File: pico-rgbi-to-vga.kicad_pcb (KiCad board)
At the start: 2 copper layers, 69 x 52 mm, 3 parts, among them J1 SDS-80J, J2 DB15_Female_HighDensity, U1 Pico

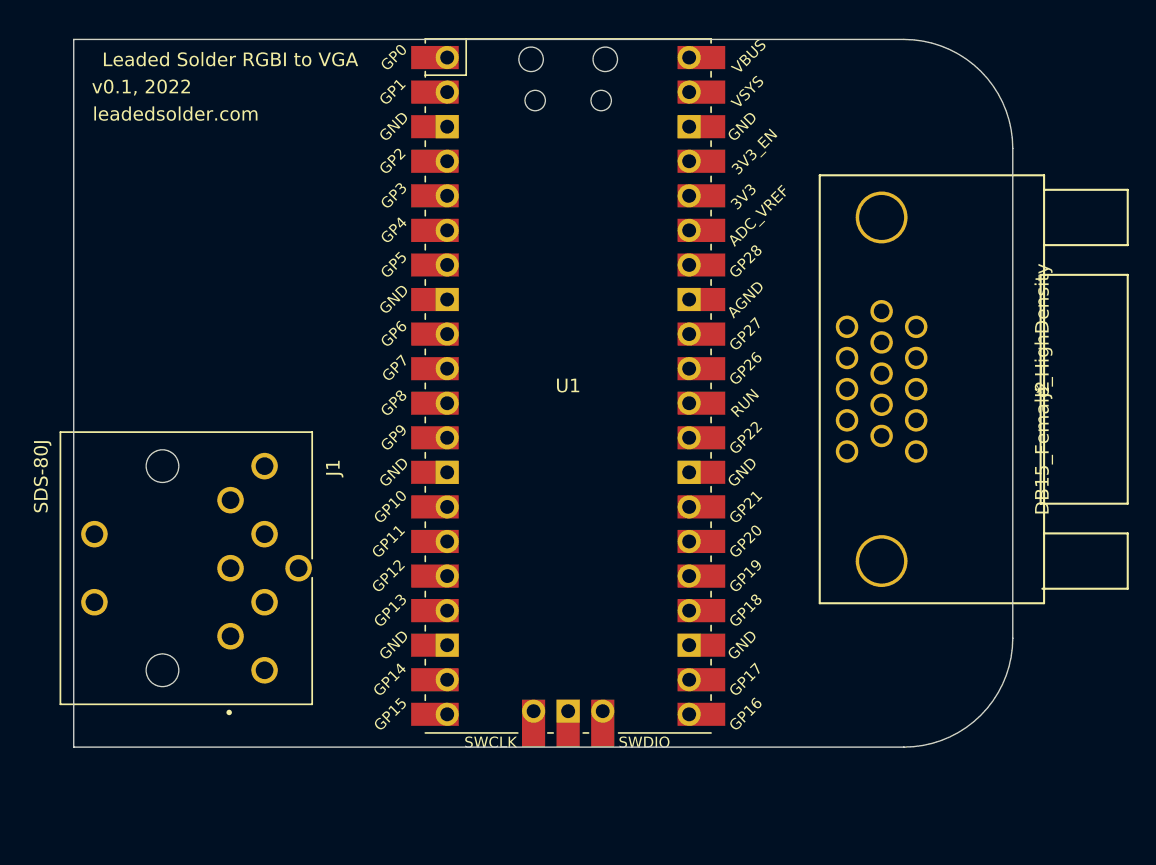
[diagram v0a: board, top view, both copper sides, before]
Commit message: Ground plane, bigger board
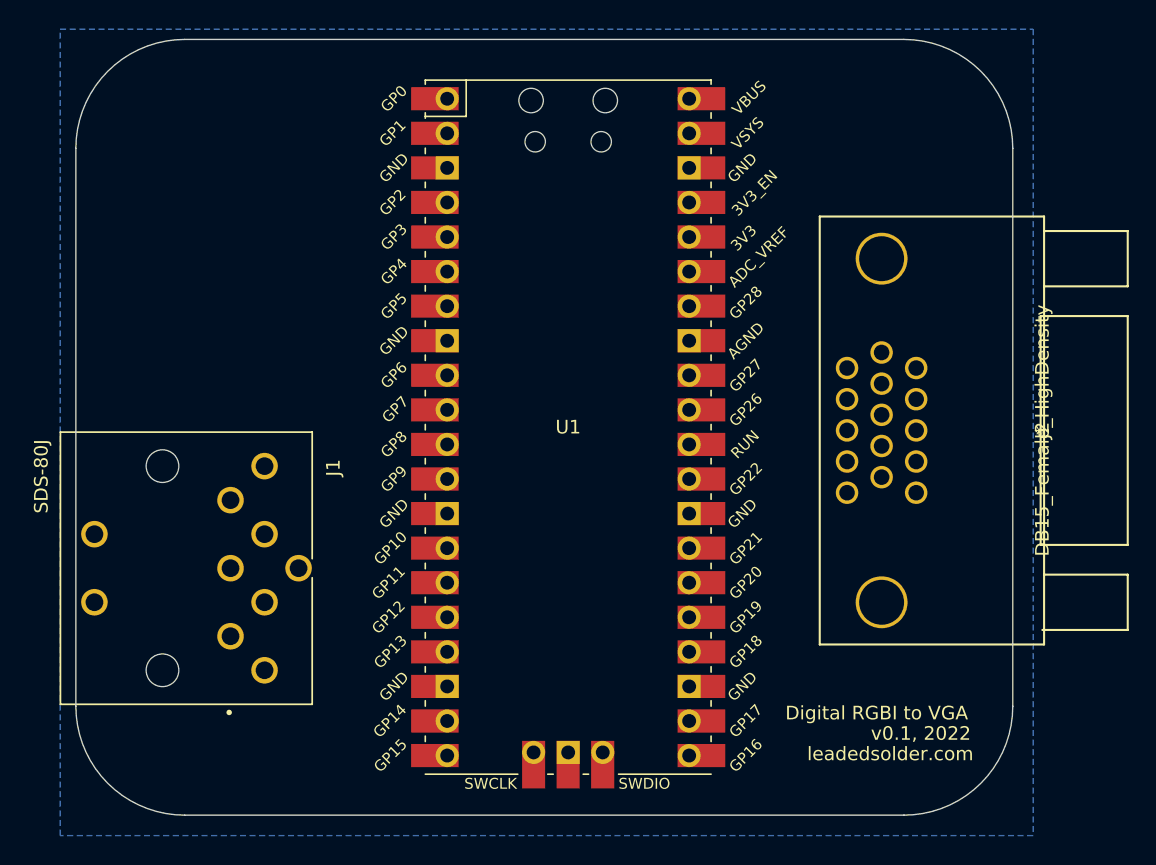
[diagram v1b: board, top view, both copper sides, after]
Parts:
- moved J2 3.03 mm to (172.2, 91.7)
- moved U1 3.03 mm to (137.3, 91.5)
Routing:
- added copper zone on B.Cu, net GND
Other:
- board size 69 x 52 mm -> 68.8 x 57 mm
- board text added: "Digital RGBI to VGA"
- board text removed: "Leaded Solder RGBI to VGA"
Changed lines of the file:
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@@
   (net 51 "unconnected-(U1-Pad43)")
   (footprint "MCU_RaspberryPi_and_Boards:RPi_Pico_SMD_TH" (layer "F.Cu")
-    (at 137.332 88.461)
+    (at 137.332 91.49)
     (descr "Through hole straight pin header, 2x20, 2.54mm pitch, double rows")
     (tags "Through hole pin header THT 2x20 2.54mm double row")
@@
   )
   (footprint "Connector_TE_AMP_HD15:FIXED-1-1734530-1" (layer "F.Cu")
-    (at 172.1739 88.706 -90)
+    (at 172.1739 91.735 -90)
     (property "Sheetfile" "pico-rgbi-to-vga.kicad_sch")
     (property "Sheetname" "")
@@
       (net 2 "GND") (pinfunction "SHIELD") (pintype "passive"))
   )
-  (gr_line (start 170 71) (end 170 107) (layer "Edge.Cuts") (width 0.1))
-  (gr_line (start 101 115) (end 101 63) (layer "Edge.Cuts") (width 0.1))
-  (gr_arc (start 170 107) (mid 167.656854 112.656854) (end 162 115) (layer "Edge.Cuts") (width 0.1))
-  (gr_line (start 162 115) (end 101 115) (layer "Edge.Cuts") (width 0.1))
-  (gr_line (start 162 63) (end 101 63) (layer "Edge.Cuts") (width 0.1))
+  (gr_arc (start 109.156854 120) (mid 103.5 117.656854) (end 101.156854 112) (layer "Edge.Cuts") (width 0.1))
+  (gr_arc (start 101.156854 70.999999) (mid 103.5 65.343145) (end 109.156854 62.999999) (layer "Edge.Cuts") (width 0.1))
+  (gr_line (start 101.156854 70.999999) (end 101.156854 112) (layer "Edge.Cuts") (width 0.1))
+  (gr_line (start 109.156854 62.999999) (end 162 63) (layer "Edge.Cuts") (width 0.1))
+  (gr_arc (start 170 112) (mid 167.656854 117.656854) (end 162 120) (layer "Edge.Cuts") (width 0.1))
+  (gr_line (start 162 120) (end 109.156854 120) (layer "Edge.Cuts") (width 0.1))
   (gr_arc (start 162 63) (mid 167.656854 65.343146) (end 170 71) (layer "Edge.Cuts") (width 0.1))
-  (gr_text "v0.1, 2022" (at 106 66.5) (layer "F.SilkS")
+  (gr_line (start 170 71) (end 170 112) (layer "Edge.Cuts") (width 0.1))
+  (gr_text "v0.1, 2022" (at 163.25 114) (layer "F.SilkS")
     (effects (font (size 1 1) (thickness 0.15)))
   )
-  (gr_text "Leaded Solder RGBI to VGA" (at 112.5 64.5) (layer "F.SilkS")
+  (gr_text "Digital RGBI to VGA" (at 160 112.5) (layer "F.SilkS")
     (effects (font (size 1 1) (thickness 0.15)))
   )
-  (gr_text "leadedsolder.com" (at 108.5 68.5) (layer "F.SilkS")
+  (gr_text "leadedsolder.com" (at 161 115.5) (layer "F.SilkS")
     (effects (font (size 1 1) (thickness 0.15)))
   )
+  (zone (net 2) (net_name "GND") (layer "B.Cu") (hatch edge 0.508)
+    (connect_pads yes (clearance 0.508))
+    (min_thickness 0.254) (filled_areas_thickness no)
+    (fill yes (thermal_gap 0.508) (thermal_bridge_width 0.508))
+    (polygon
+      (pts
+        (xy 171.5 121.5)
+        (xy 100 121.5)
+        (xy 100 62.25)
+        (xy 171.5 62.25)
+      )
+    )
+  )
 )

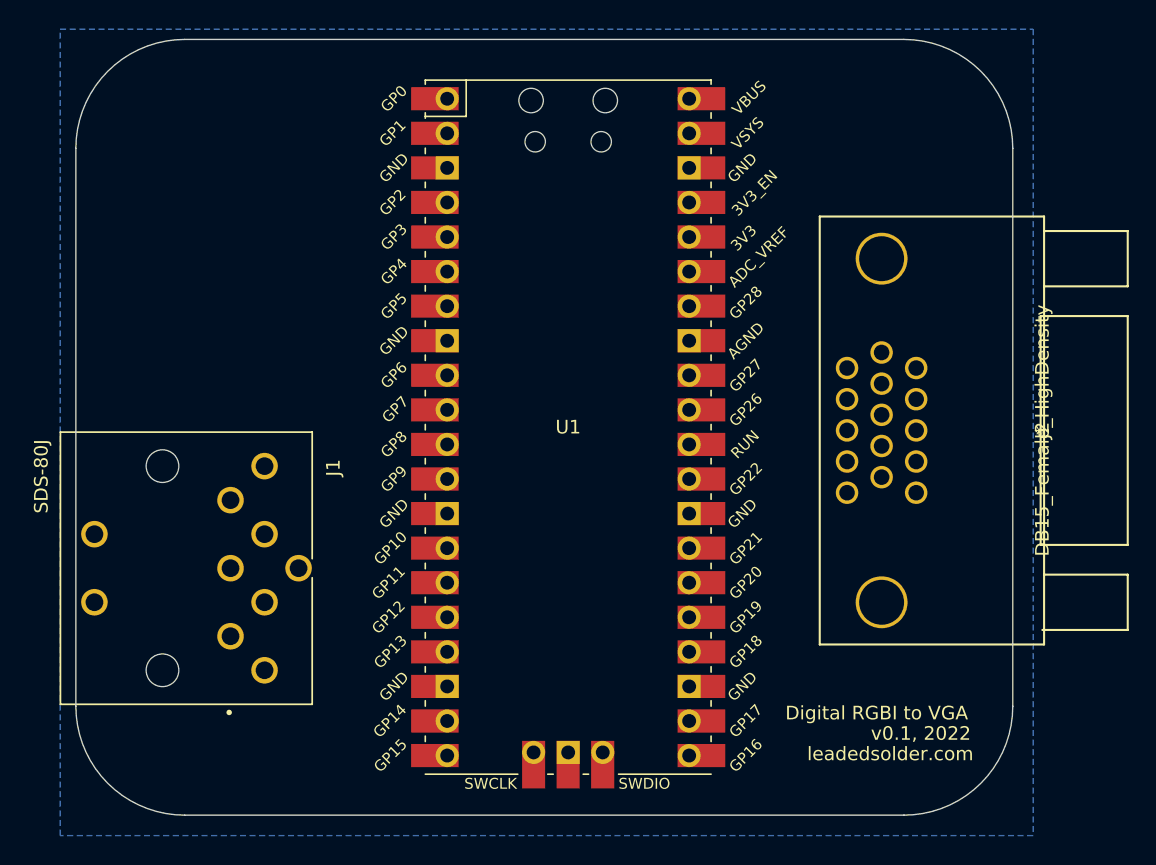
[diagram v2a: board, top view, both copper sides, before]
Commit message: Basic left-side implementation with voltage divider
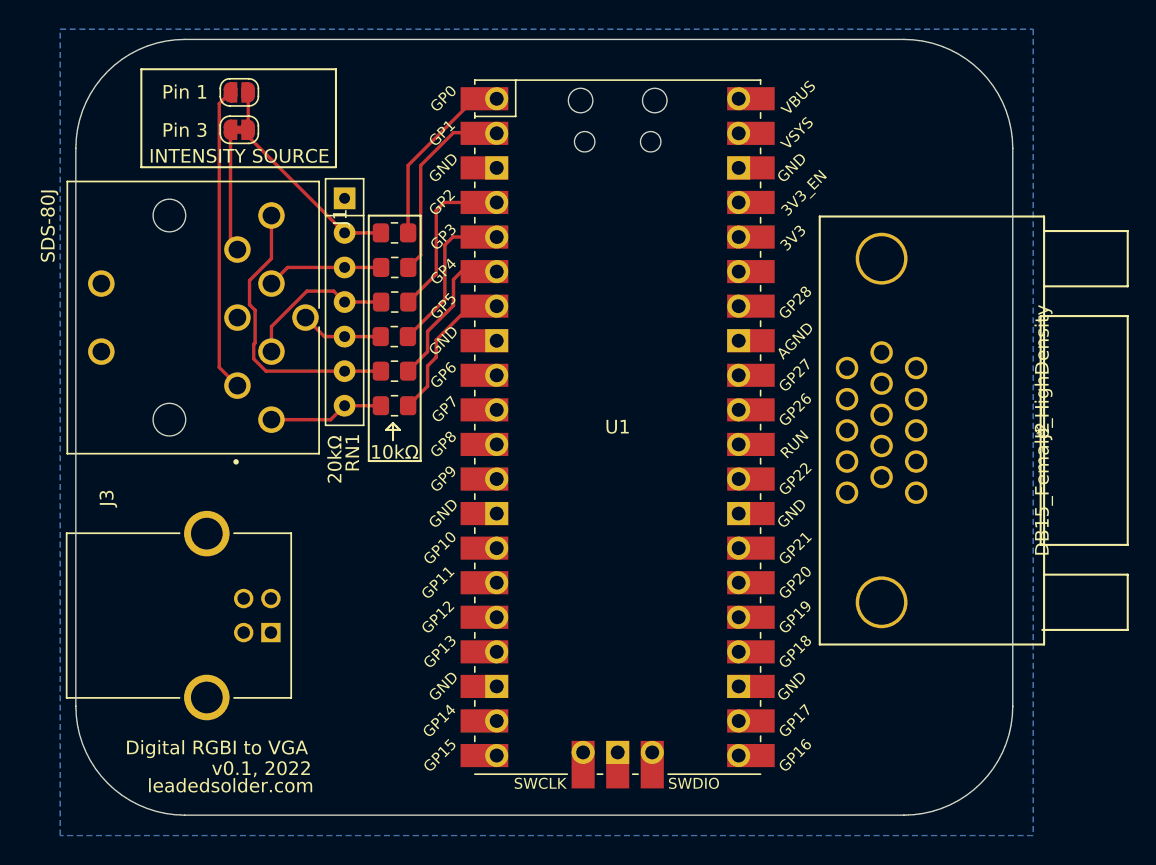
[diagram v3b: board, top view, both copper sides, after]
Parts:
- added J3: USB-B1HSB6, USB-B1HSB6:OST_USB-B1HSB6, F.Cu at (110.8, 105.3)
- added JP1: Jumper_2_Open, Jumper:SolderJumper-2_P1.3mm_Open_RoundedPad1.0x1.5mm, F.Cu at (113.2, 66.9)
- added JP2: Jumper_2_Bridged, Jumper:SolderJumper-2_P1.3mm_Bridged_RoundedPad1.0x1.5mm, F.Cu at (113.2, 69.6)
- added R1: 10kΩ, Resistor_SMD:R_0805_2012Metric_Pad1.20x1.40mm_HandSolder, F.Cu at (124.6, 89.9)
- added R2: 10kΩ, Resistor_SMD:R_0805_2012Metric_Pad1.20x1.40mm_HandSolder, F.Cu at (124.6, 87.4)
- added R3: 10kΩ, Resistor_SMD:R_0805_2012Metric_Pad1.20x1.40mm_HandSolder, F.Cu at (124.6, 84.8)
- added R4: 10kΩ, Resistor_SMD:R_0805_2012Metric_Pad1.20x1.40mm_HandSolder, F.Cu at (124.6, 82.3)
- added R5: 10kΩ, Resistor_SMD:R_0805_2012Metric_Pad1.20x1.40mm_HandSolder, F.Cu at (124.6, 79.8)
- added R6: 10kΩ, Resistor_SMD:R_0805_2012Metric_Pad1.20x1.40mm_HandSolder, F.Cu at (124.6, 77.2)
- added RN1: 20kΩ, Resistor_THT:R_Array_SIP7, F.Cu at (120.9, 74.7)
- moved J1 18.4 mm to (113.0, 83.4)
- moved U1 3.64 mm to (141.0, 91.5)
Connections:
- J1 pad 1: unconnected-(J1-Pad1) -> Net-(J1-Pad1)
- J1 pad 3: /INTENS_IN -> Net-(J1-Pad3)
- U1 pad 1: unconnected-(U1-Pad1) -> /INTENS_3v3
- U1 pad 2: unconnected-(U1-Pad2) -> /VSYNC_3v3
- U1 pad 4: unconnected-(U1-Pad4) -> /HSYNC_3v3
- U1 pad 40: unconnected-(U1-Pad40) -> +5V
- U1 pad 5: unconnected-(U1-Pad5) -> /BLUE_3v3
- U1 pad 6: unconnected-(U1-Pad6) -> /GREEN_3v3
- U1 pad 7: unconnected-(U1-Pad7) -> /RED_3v3
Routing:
- net Net-(J1-Pad1): track 0.00 -> 22.4 mm
- net /GREEN_IN: track 0.00 -> 21.1 mm
- net /INTENS_IN: track 0.00 -> 15.9 mm
- net /VSYNC_3v3: track 0.00 -> 14.5 mm
- net /INTENS_3v3: track 0.00 -> 13.5 mm
- net /HSYNC_3v3: track 0.00 -> 12.3 mm
- net /BLUE_3v3: track 0.00 -> 11.9 mm
- net /GREEN_3v3: track 0.00 -> 11.5 mm
- net /HSYNC_IN: track 0.00 -> 11.3 mm
- net /RED_3v3: track 0.00 -> 11.2 mm
- net Net-(J1-Pad3): track 0.00 -> 9.01 mm
- net /VSYNC_IN: track 0.00 -> 8.55 mm
- net /RED_IN: track 0.00 -> 8.46 mm
- net /BLUE_IN: track 0.00 -> 6.10 mm
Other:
- board text added: "INTENSITY SOURCE"
- board text added: "Pin 1"
- board text added: "Pin 3"

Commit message: Power LED, output voltage divider
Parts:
- added D1: LED, LED_THT:LED_D3.0mm, F.Cu at (122.2, 112.0)
- added R10: 8.2kΩ, Resistor_SMD:R_0805_2012Metric_Pad1.20x1.40mm_HandSolder, F.Cu at (163.8, 110.0)
- added R11: 8.2kΩ, Resistor_SMD:R_0805_2012Metric_Pad1.20x1.40mm_HandSolder, F.Cu at (161.3, 110.0)
- added R12: 8.2kΩ, Resistor_SMD:R_0805_2012Metric_Pad1.20x1.40mm_HandSolder, F.Cu at (158.8, 110.0)
- added R13: 1kΩ, Resistor_SMD:R_0805_2012Metric_Pad1.20x1.40mm_HandSolder, F.Cu at (122.2, 105.7)
- added R7: 2.2kΩ, Resistor_SMD:R_0805_2012Metric_Pad1.20x1.40mm_HandSolder, F.Cu at (163.8, 114.0)
- added R8: 2.2kΩ, Resistor_SMD:R_0805_2012Metric_Pad1.20x1.40mm_HandSolder, F.Cu at (161.3, 114.0)
- added R9: 2.2kΩ, Resistor_SMD:R_0805_2012Metric_Pad1.20x1.40mm_HandSolder, F.Cu at (158.8, 114.0)
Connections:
- U1 pad 21: unconnected-(U1-Pad21) -> /VGA_3v3_RED
- U1 pad 22: unconnected-(U1-Pad22) -> /VGA_3v3_GREEN
- U1 pad 24: unconnected-(U1-Pad24) -> /VGA_3v3_BLUE
- U1 pad 25: unconnected-(U1-Pad25) -> /VGA_3v3_HSYNC
- U1 pad 26: unconnected-(U1-Pad26) -> /VGA_3v3_VSYNC
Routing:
- net /RED_OUT: track 0.00 -> 31.5 mm
- net /VGA_3v3_RED: track 0.00 -> 23.3 mm
- net /GREEN_OUT: track 0.00 -> 22.5 mm
- net /VGA_3v3_GREEN: track 0.00 -> 19.3 mm
- net /BLUE_OUT: track 0.00 -> 18.7 mm
- net /VGA_3v3_BLUE: track 0.00 -> 14.5 mm
- net +5V: track 0.00 -> 6.05 mm
- net Net-(D1-Pad2): track 0.00 -> 4.22 mm
- net GND: track 0.00 -> 3.49 mm, vias 0 -> 4
- net /RED_3v3: track 11.2 -> 11.9 mm
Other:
- board text added: "POWER"

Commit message: Power plane
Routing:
- net /VGA_3v3_BLUE: track 14.5 -> 13.8 mm
- net GND: vias 4 -> 3
- added copper zone on F.Cu, net +5V
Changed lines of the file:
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@@
     (property "Sheetname" "")
     (attr through_hole)
-    (fp_text reference "J3" (at -8.638335 7.327875 90) (layer "F.SilkS")
+    (fp_text reference "J3" (at 0.076 0.036 90) (layer "F.SilkS")
       (effects (font (size 1.000386 1.000386) (thickness 0.15)))
     )
-    (fp_text value "USB-B1HSB6" (at 8.72573 1.61198 90) (layer "F.Fab")
+    (fp_text value "USB-B1HSB6" (at 0.076 2.068 90) (layer "F.SilkS")
       (effects (font (size 1.001228 1.001228) (thickness 0.15)))
     )
@@
     (property "Sheetname" "")
     (attr through_hole)
-    (fp_text reference "J2" (at 0 0 90) (layer "F.SilkS")
-      (effects (font (size 1 1) (thickness 0.15)))
-    )
-    (fp_text value "DB15_Female_HighDensity" (at 0 0 90) (layer "F.SilkS")
-      (effects (font (size 1 1) (thickness 0.15)))
-    )
-    (fp_text user "*" (at 0 0 90) (layer "F.SilkS")
+    (fp_text reference "J2" (at 0 3.7719 90) (layer "F.SilkS")
+      (effects (font (size 1 1) (thickness 0.15)))
+    )
+    (fp_text value "DB15_Female_HighDensity" (at 0 0 90) (layer "F.SilkS") hide
+      (effects (font (size 1 1) (thickness 0.15)))
+    )
+    (fp_text user "*" (at 0 0 90) (layer "F.SilkS") hide
       (effects (font (size 1 1) (thickness 0.15)))
     )
@@
     (attr through_hole exclude_from_pos_files)
     (fp_text reference "J1" (at -5.207 -4.826 90) (layer "F.SilkS")
-      (effects (font (size 1.00263 1.00263) (thickness 0.05)))
-    )
-    (fp_text value "SDS-80J" (at -6.74273 13.9016 90) (layer "F.SilkS")
-      (effects (font (size 1.00263 1.00263) (thickness 0.05)))
+      (effects (font (size 1.00263 1.00263) (thickness 0.15)))
+    )
+    (fp_text value "SDS-80J" (at 0 3.429 90) (layer "F.SilkS")
+      (effects (font (size 1.00263 1.00263) (thickness 0.15)))
     )
     (fp_line (start -10 -6) (end -10 12.5) (layer "F.SilkS") (width 0.127))
@@
   (segment (start 161.29 115.046) (end 161.29 116.205) (width 1) (layer "F.Cu") (net 2))
   (segment (start 158.75 115.03) (end 158.75 116.205) (width 1) (layer "F.Cu") (net 2))
-  (via (at 161.29 116.205) (size 0.8) (drill 0.4) (layers "F.Cu" "B.Cu") (net 2))
   (via (at 158.75 116.205) (size 0.8) (drill 0.4) (layers "F.Cu" "B.Cu") (net 2))
   (via (at 163.83 116.205) (size 0.8) (drill 0.4) (layers "F.Cu" "B.Cu") (net 2))
@@
   (segment (start 125.571 72.009978) (end 125.571 77.216) (width 0.5) (layer "F.Cu") (net 49))
   (segment (start 165.1 114.316) (end 163.83 113.046) (width 0.5) (layer "F.Cu") (net 50))
-  (segment (start 149.86 115.62) (end 152.41451 118.17451) (width 0.5) (layer "F.Cu") (net 50))
+  (segment (start 151.561 115.62) (end 154.178 118.237) (width 0.5) (layer "F.Cu") (net 50))
+  (segment (start 163.703 118.237) (end 165.1 116.84) (width 0.5) (layer "F.Cu") (net 50))
   (segment (start 165.1 116.84) (end 165.1 114.316) (width 0.5) (layer "F.Cu") (net 50))
-  (segment (start 152.41451 118.17451) (end 163.76549 118.17451) (width 0.5) (layer "F.Cu") (net 50))
+  (segment (start 154.178 118.237) (end 163.703 118.237) (width 0.5) (layer "F.Cu") (net 50))
   (segment (start 163.83 113.046) (end 163.83 110.966) (width 0.5) (layer "F.Cu") (net 50))
-  (segment (start 163.76549 118.17451) (end 165.1 116.84) (width 0.5) (layer "F.Cu") (net 50))
+  (segment (start 149.86 115.62) (end 151.561 115.62) (width 0.5) (layer "F.Cu") (net 50))
   (segment (start 161.29 113.046) (end 161.29 110.998) (width 0.5) (layer "F.Cu") (net 51))
-  (segment (start 160.02 114.316) (end 161.29 113.046) (width 0.5) (layer "F.Cu") (net 51))
-  (segment (start 153.67 115.030978) (end 153.67 116.205) (width 0.5) (layer "F.Cu") (net 51))
-  (segment (start 153.67 116.205) (end 154.94 117.475) (width 0.5) (layer "F.Cu") (net 51))
-  (segment (start 154.94 117.475) (end 159.385 117.475) (width 0.5) (layer "F.Cu") (net 51))
-  (segment (start 160.02 116.84) (end 160.02 114.316) (width 0.5) (layer "F.Cu") (net 51))
-  (segment (start 149.86 113.08) (end 151.719022 113.08) (width 0.5) (layer "F.Cu") (net 51))
-  (segment (start 151.719022 113.08) (end 153.67 115.030978) (width 0.5) (layer "F.Cu") (net 51))
-  (segment (start 159.385 117.475) (end 160.02 116.84) (width 0.5) (layer "F.Cu") (net 51))
-  (segment (start 153.67 112.395) (end 154.305 113.03) (width 0.5) (layer "F.Cu") (net 52))
-  (segment (start 154.305 113.03) (end 158.75 113.03) (width 0.5) (layer "F.Cu") (net 52))
-  (segment (start 151.719022 108) (end 153.67 109.950978) (width 0.5) (layer "F.Cu") (net 52))
-  (segment (start 149.86 108) (end 151.719022 108) (width 0.5) (layer "F.Cu") (net 52))
+  (segment (start 160.02 116.332) (end 159.131 117.221) (width 0.5) (layer "F.Cu") (net 51))
+  (segment (start 153.416 114.554) (end 151.942 113.08) (width 0.5) (layer "F.Cu") (net 51))
+  (segment (start 160.02 114.316) (end 160.02 116.332) (width 0.5) (layer "F.Cu") (net 51))
+  (segment (start 159.131 117.221) (end 154.813 117.221) (width 0.5) (layer "F.Cu") (net 51))
+  (segment (start 154.813 117.221) (end 153.416 115.824) (width 0.5) (layer "F.Cu") (net 51))
+  (segment (start 151.942 113.08) (end 149.86 113.08) (width 0.5) (layer "F.Cu") (net 51))
+  (segment (start 161.29 113.046) (end 160.02 114.316) (width 0.5) (layer "F.Cu") (net 51))
+  (segment (start 153.416 115.824) (end 153.416 114.554) (width 0.5) (layer "F.Cu") (net 51))
+  (segment (start 158.75 113.03) (end 155.448 113.03) (width 0.5) (layer "F.Cu") (net 52))
+  (segment (start 154.051 110.331978) (end 151.719022 108) (width 0.5) (layer "F.Cu") (net 52))
+  (segment (start 155.448 113.03) (end 154.051 111.633) (width 0.5) (layer "F.Cu") (net 52))
+  (segment (start 154.051 111.633) (end 154.051 110.331978) (width 0.5) (layer "F.Cu") (net 52))
   (segment (start 158.75 113.03) (end 158.75 110.95) (width 0.5) (layer "F.Cu") (net 52))
-  (segment (start 153.67 109.950978) (end 153.67 112.395) (width 0.5) (layer "F.Cu") (net 52))
+  (segment (start 151.719022 108) (end 149.86 108) (width 0.5) (layer "F.Cu") (net 52))
   (segment (start 123.158 105.664) (end 123.158 108.49) (width 1) (layer "F.Cu") (net 55))
   (segment (start 123.158 108.49) (end 122.174 109.474) (width 1) (layer "F.Cu") (net 55))
+  (zone (net 41) (net_name "+5V") (layer "F.Cu") (hatch edge 0.508)
+    (connect_pads (clearance 0.508))
+    (min_thickness 0.254) (filled_areas_thickness no)
+    (fill yes (thermal_gap 0.508) (thermal_bridge_width 0.508))
+    (polygon
+      (pts
+        (xy 171.958 62.23)
+        (xy 171.577 121.539)
+        (xy 99.949 121.666)
+        (xy 99.822 62.103)
+      )
+    )
+  )
   (zone (net 0) (net_name "") (layer "F.Cu") (hatch edge 0.508)
     (connect_pads (clearance 0))

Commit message: Fully laid out, I think
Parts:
- added Q1: 2n2222, Package_TO_SOT_THT:TO-92_Inline, F.Cu at (158.7, 71.4)
- added Q2: 2n2222, Package_TO_SOT_THT:TO-92_Inline, F.Cu at (164.4, 71.4)
- added R14: 1kΩ, Resistor_SMD:R_0805_2012Metric_Pad1.20x1.40mm_HandSolder, F.Cu at (160.0, 67.6)
- added R15: 10kΩ, Resistor_SMD:R_0805_2012Metric_Pad1.20x1.40mm_HandSolder, F.Cu at (159.9, 74.4)
- added R16: 1kΩ, Resistor_SMD:R_0805_2012Metric_Pad1.20x1.40mm_HandSolder, F.Cu at (165.7, 67.6)
- added R17: 10kΩ, Resistor_SMD:R_0805_2012Metric_Pad1.20x1.40mm_HandSolder, F.Cu at (165.7, 74.4)
- added SW1: SW_Push, Button_Switch_THT:SW_PUSH_6mm, F.Cu at (119.0, 97.7)
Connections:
- U1 pad 20: unconnected-(U1-Pad20) -> /SW_PALETTE_CHANGE
- U1 pad 36: unconnected-(U1-Pad36) -> +3V3
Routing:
- net +5V: track 6.05 -> 179.7 mm, vias 0 -> 3
- net /VGA_3v3_VSYNC: track 0.00 -> 44.1 mm
- net /VGA_3v3_HSYNC: track 0.00 -> 40.7 mm
- net +3V3: track 0.00 -> 30.2 mm
- net /VSYNC_OUT: track 0.00 -> 24.3 mm
- net /SW_PALETTE_CHANGE: track 0.00 -> 23.6 mm
- net /HSYNC_OUT: track 0.00 -> 22.3 mm
- net Net-(Q2-Pad2): track 0.00 -> 6.99 mm, vias 0 -> 1
- net Net-(Q1-Pad2): track 0.00 -> 6.52 mm, vias 0 -> 1
